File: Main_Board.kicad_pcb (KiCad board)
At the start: 2 copper layers, 95 x 95 mm, 61 parts, among them J1 DAC_12-bits, J2 Measurement_Header, Q1 Q_PNP_BCE, Q2 Q_NPN_BCE, U1 AD667, U2 LF356

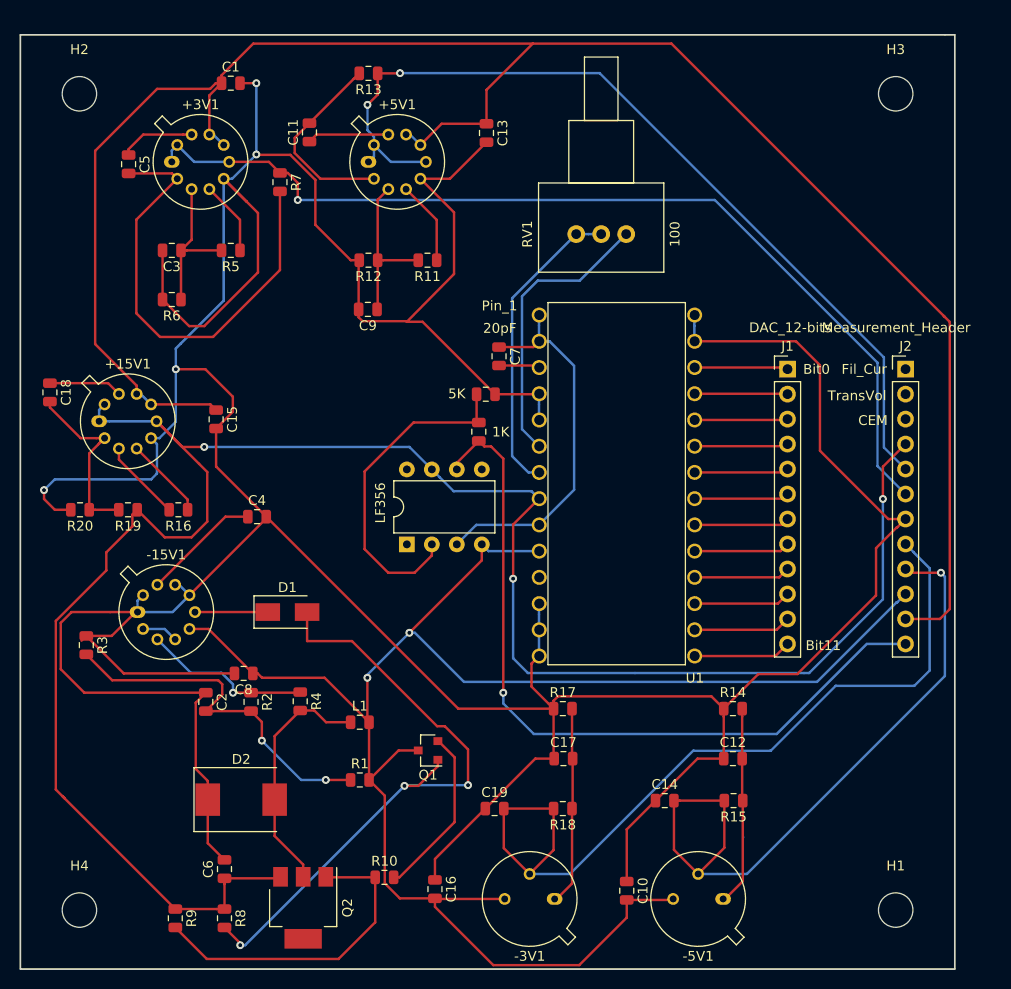
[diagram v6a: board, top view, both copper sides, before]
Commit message: Shortened to 9cm
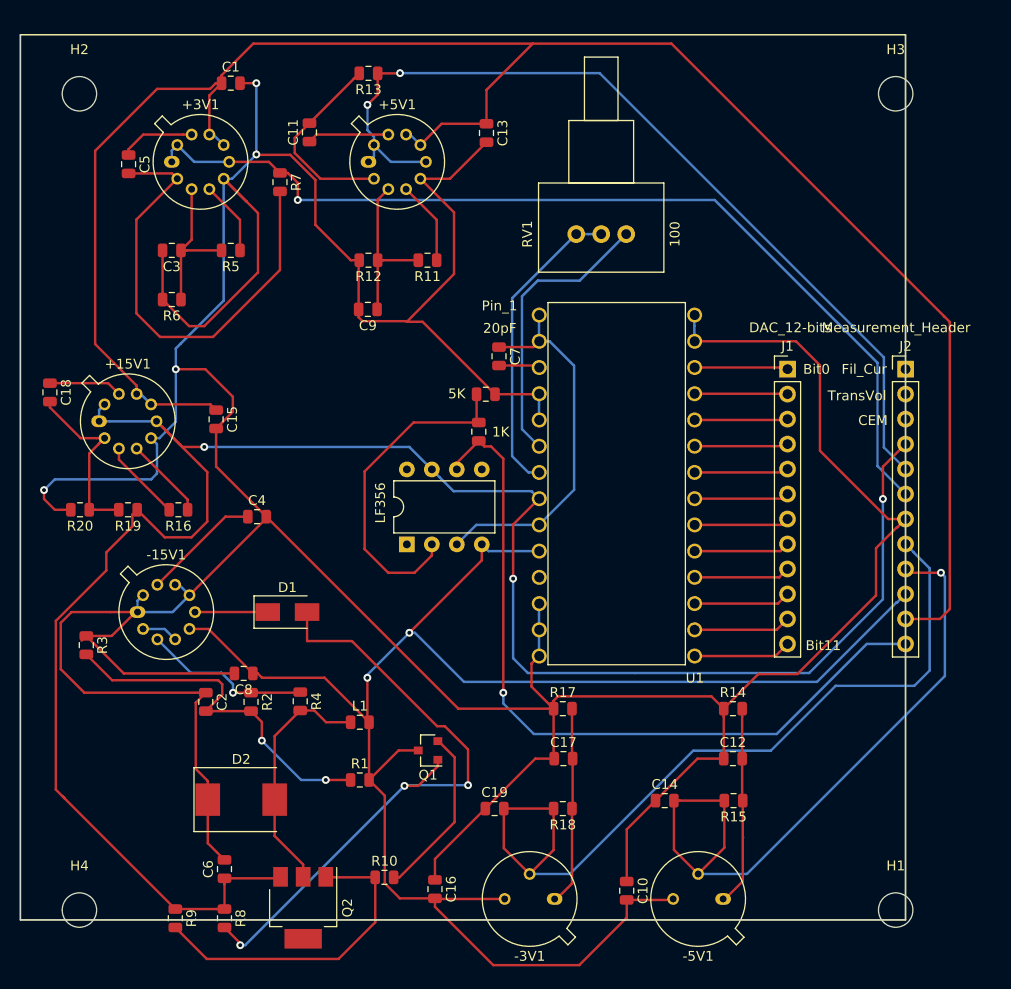
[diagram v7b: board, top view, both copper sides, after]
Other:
- board size 95 x 95 mm -> 90 x 90 mm
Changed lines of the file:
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@@
-(kicad_pcb (version 20171130) (host pcbnew "(5.1.5)-3")
+(kicad_pcb (version 20171130) (host pcbnew "(5.1.4)-1")
   (general
     (thickness 1.6)
-    (drawings 17)
+    (drawings 15)
     (tracks 503)
     (zones 0)
@@
     )
   )
+  (dimension 90 (width 0.15) (layer F.SilkS)
+    (gr_text "90.000 mm" (at 4.7 126 90) (layer F.SilkS)
+      (effects (font (size 1 1) (thickness 0.15)))
+    )
+    (feature1 (pts (xy 12 81) (xy 5.413579 81)))
+    (feature2 (pts (xy 12 171) (xy 5.413579 171)))
+    (crossbar (pts (xy 6 171) (xy 6 81)))
+    (arrow1a (pts (xy 6 81) (xy 6.586421 82.126504)))
+    (arrow1b (pts (xy 6 81) (xy 5.413579 82.126504)))
+    (arrow2a (pts (xy 6 171) (xy 6.586421 169.873496)))
+    (arrow2b (pts (xy 6 171) (xy 5.413579 169.873496)))
+  )
+  (dimension 90 (width 0.15) (layer F.SilkS)
+    (gr_text "90.000 mm" (at 57 179.3) (layer F.SilkS)
+      (effects (font (size 1 1) (thickness 0.15)))
+    )
+    (feature1 (pts (xy 102 171) (xy 102 178.586421)))
+    (feature2 (pts (xy 12 171) (xy 12 178.586421)))
+    (crossbar (pts (xy 12 178) (xy 102 178)))
+    (arrow1a (pts (xy 102 178) (xy 100.873496 178.586421)))
+    (arrow1b (pts (xy 102 178) (xy 100.873496 177.413579)))
+    (arrow2a (pts (xy 12 178) (xy 13.126504 178.586421)))
+    (arrow2b (pts (xy 12 178) (xy 13.126504 177.413579)))
+  )
+  (gr_line (start 102 171) (end 102 81) (layer Edge.Cuts) (width 0.1))
+  (gr_line (start 12 171) (end 102 171) (layer Edge.Cuts) (width 0.1))
+  (gr_line (start 12 81) (end 12 171) (layer Edge.Cuts) (width 0.1))
+  (gr_line (start 102 81) (end 12 81) (layer F.SilkS) (width 0.15))
+  (gr_line (start 102 171) (end 102 81) (layer F.SilkS) (width 0.15))
+  (gr_line (start 12 171) (end 102 171) (layer F.SilkS) (width 0.15))
+  (gr_line (start 12 81) (end 12 171) (layer F.SilkS) (width 0.15))
   (gr_text Fil_Cur (at 97.8012 115.0106) (layer F.SilkS)
     (effects (font (size 1 1) (thickness 0.15)))
@@
     (effects (font (size 1 1) (thickness 0.15)))
   )
-  (gr_line (start 107 81) (end 12 81) (layer Edge.Cuts) (width 0.1))
-  (gr_line (start 107 176) (end 107 81) (layer Edge.Cuts) (width 0.1))
-  (gr_line (start 12 176) (end 107 176) (layer Edge.Cuts) (width 0.1))
-  (gr_line (start 12 81) (end 12 176) (layer Edge.Cuts) (width 0.1))
-  (gr_line (start 107 81) (end 106 81) (layer F.SilkS) (width 0.15))
-  (gr_line (start 107 176) (end 107 81) (layer F.SilkS) (width 0.15))
-  (gr_line (start 12 176) (end 12 81) (layer F.SilkS) (width 0.15))
-  (gr_line (start 107 176) (end 12 176) (layer F.SilkS) (width 0.15))
-  (gr_line (start 12 81) (end 106 81) (layer F.SilkS) (width 0.15))
-  (dimension 95 (width 0.15) (layer F.SilkS)
-    (gr_text "95.000 mm" (at 59.5 185.3) (layer F.SilkS)
-      (effects (font (size 1 1) (thickness 0.15)))
-    )
-    (feature1 (pts (xy 107 176) (xy 107 184.586421)))
-    (feature2 (pts (xy 12 176) (xy 12 184.586421)))
-    (crossbar (pts (xy 12 184) (xy 107 184)))
-    (arrow1a (pts (xy 107 184) (xy 105.873496 184.586421)))
-    (arrow1b (pts (xy 107 184) (xy 105.873496 183.413579)))
-    (arrow2a (pts (xy 12 184) (xy 13.126504 184.586421)))
-    (arrow2b (pts (xy 12 184) (xy 13.126504 183.413579)))
-  )
-  (dimension 95 (width 0.15) (layer F.SilkS)
-    (gr_text "95.000 mm" (at 2.7 128.5 90) (layer F.SilkS)
-      (effects (font (size 1 1) (thickness 0.15)))
-    )
-    (feature1 (pts (xy 12 81) (xy 3.413579 81)))
-    (feature2 (pts (xy 12 176) (xy 3.413579 176)))
-    (crossbar (pts (xy 4 176) (xy 4 81)))
-    (arrow1a (pts (xy 4 81) (xy 4.586421 82.126504)))
-    (arrow1b (pts (xy 4 81) (xy 3.413579 82.126504)))
-    (arrow2a (pts (xy 4 176) (xy 4.586421 174.873496)))
-    (arrow2b (pts (xy 4 176) (xy 3.413579 174.873496)))
-  )
   (segment (start 23.91 138.541337) (end 24.46767 137.983667) (width 0.25) (layer B.Cu) (net 1))

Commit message: Mounting holes
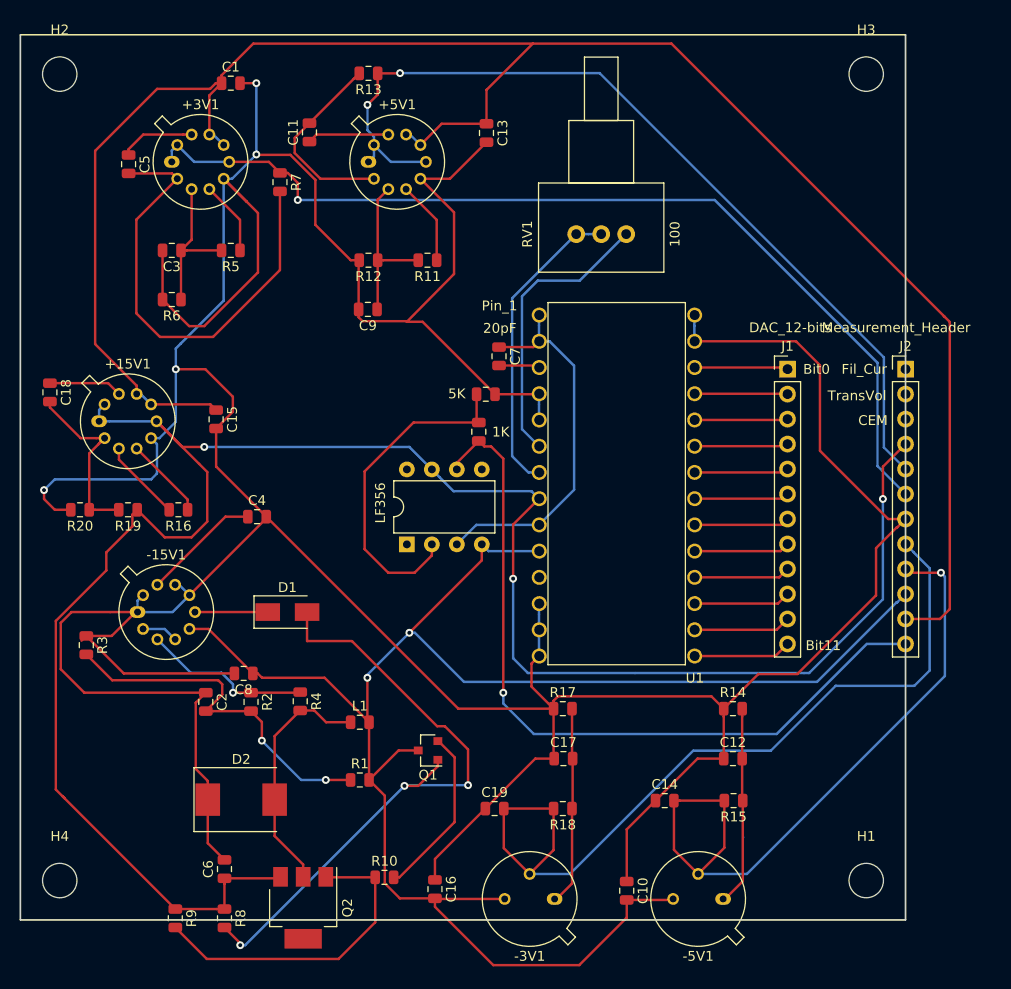
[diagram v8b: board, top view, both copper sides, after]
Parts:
- moved H1 4.24 mm to (98.0, 167.0)
- moved H3 3.61 mm to (98.0, 85.0)
- moved H4 3.61 mm to (16.0, 167.0)
- moved H2 2.83 mm to (16.0, 85.0)
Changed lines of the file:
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@@
   )
   (module MountingHole:MountingHole_3.5mm (layer F.Cu)
-    (at 18 170)
+    (at 16 167)
     (descr "Mounting Hole 3.5mm, no annular")
     (tags "mounting hole 3.5mm no annular")
@@
     (fp_circle (center 0 0) (end 3.75 0) (layer F.CrtYd) (width 0.05))
     (fp_circle (center 0 0) (end 3.5 0) (layer Cmts.User) (width 0.15))
-    (fp_text user %R (at 0.3 0) (layer F.Fab)
+    (fp_text user %R (at 0 0) (layer F.Fab)
       (effects (font (size 1 1) (thickness 0.15)))
     )
@@
   )
   (module MountingHole:MountingHole_3.5mm (layer F.Cu)
-    (at 101 87)
+    (at 98 85)
     (descr "Mounting Hole 3.5mm, no annular")
     (tags "mounting hole 3.5mm no annular")
@@
     (fp_circle (center 0 0) (end 3.75 0) (layer F.CrtYd) (width 0.05))
     (fp_circle (center 0 0) (end 3.5 0) (layer Cmts.User) (width 0.15))
-    (fp_text user %R (at 0.3 0) (layer F.Fab)
+    (fp_text user %R (at 0 0) (layer F.Fab)
       (effects (font (size 1 1) (thickness 0.15)))
     )
@@
   )
   (module MountingHole:MountingHole_3.5mm (layer F.Cu)
-    (at 18 87)
+    (at 16 85)
     (descr "Mounting Hole 3.5mm, no annular")
     (tags "mounting hole 3.5mm no annular")
@@
     (fp_circle (center 0 0) (end 3.75 0) (layer F.CrtYd) (width 0.05))
     (fp_circle (center 0 0) (end 3.5 0) (layer Cmts.User) (width 0.15))
-    (fp_text user %R (at 0.3 0) (layer F.Fab)
+    (fp_text user %R (at 0 0) (layer F.Fab)
       (effects (font (size 1 1) (thickness 0.15)))
     )
@@
   )
   (module MountingHole:MountingHole_3.5mm (layer F.Cu)
-    (at 101 170)
+    (at 98 167)
     (descr "Mounting Hole 3.5mm, no annular")
     (tags "mounting hole 3.5mm no annular")
@@
     (fp_circle (center 0 0) (end 3.75 0) (layer F.CrtYd) (width 0.05))
     (fp_circle (center 0 0) (end 3.5 0) (layer Cmts.User) (width 0.15))
-    (fp_text user %R (at -0.5964 -0.612) (layer F.Fab)
+    (fp_text user %R (at -1 0) (layer F.Fab)
       (effects (font (size 1 1) (thickness 0.15)))
     )
